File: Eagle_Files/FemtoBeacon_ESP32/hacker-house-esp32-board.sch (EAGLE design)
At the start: 56 parts, among them IC1 FT232RQ

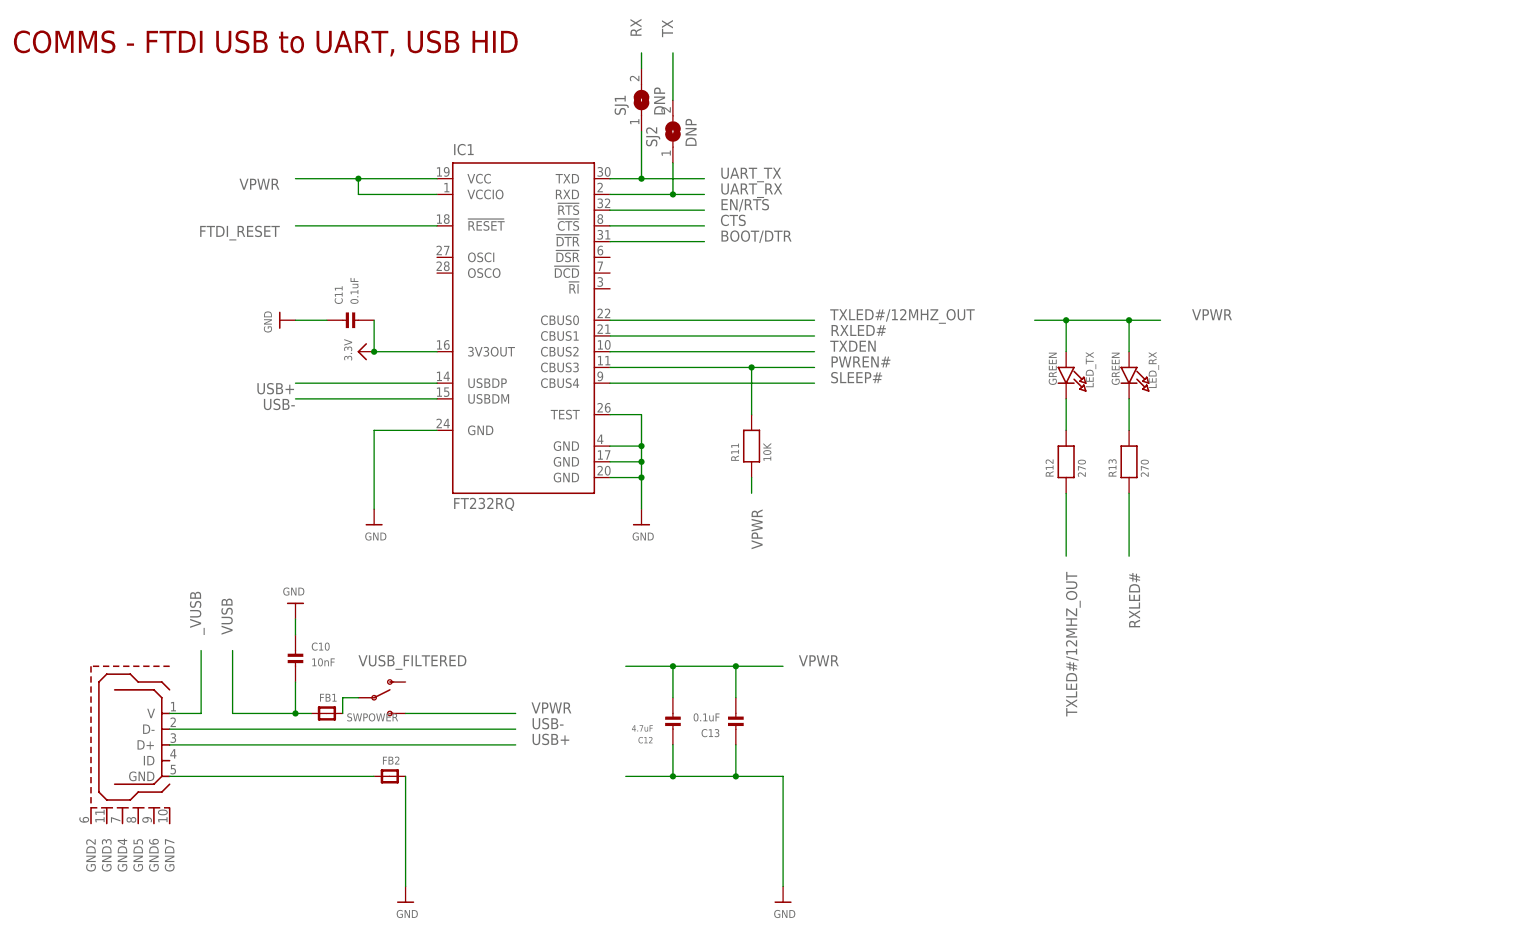
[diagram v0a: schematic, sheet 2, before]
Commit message: Revised BoM for the Hacker.House board, fixed missing 3V3 trace with 2.0.1 design of Hacker.House board (version bump to 2.0.2)
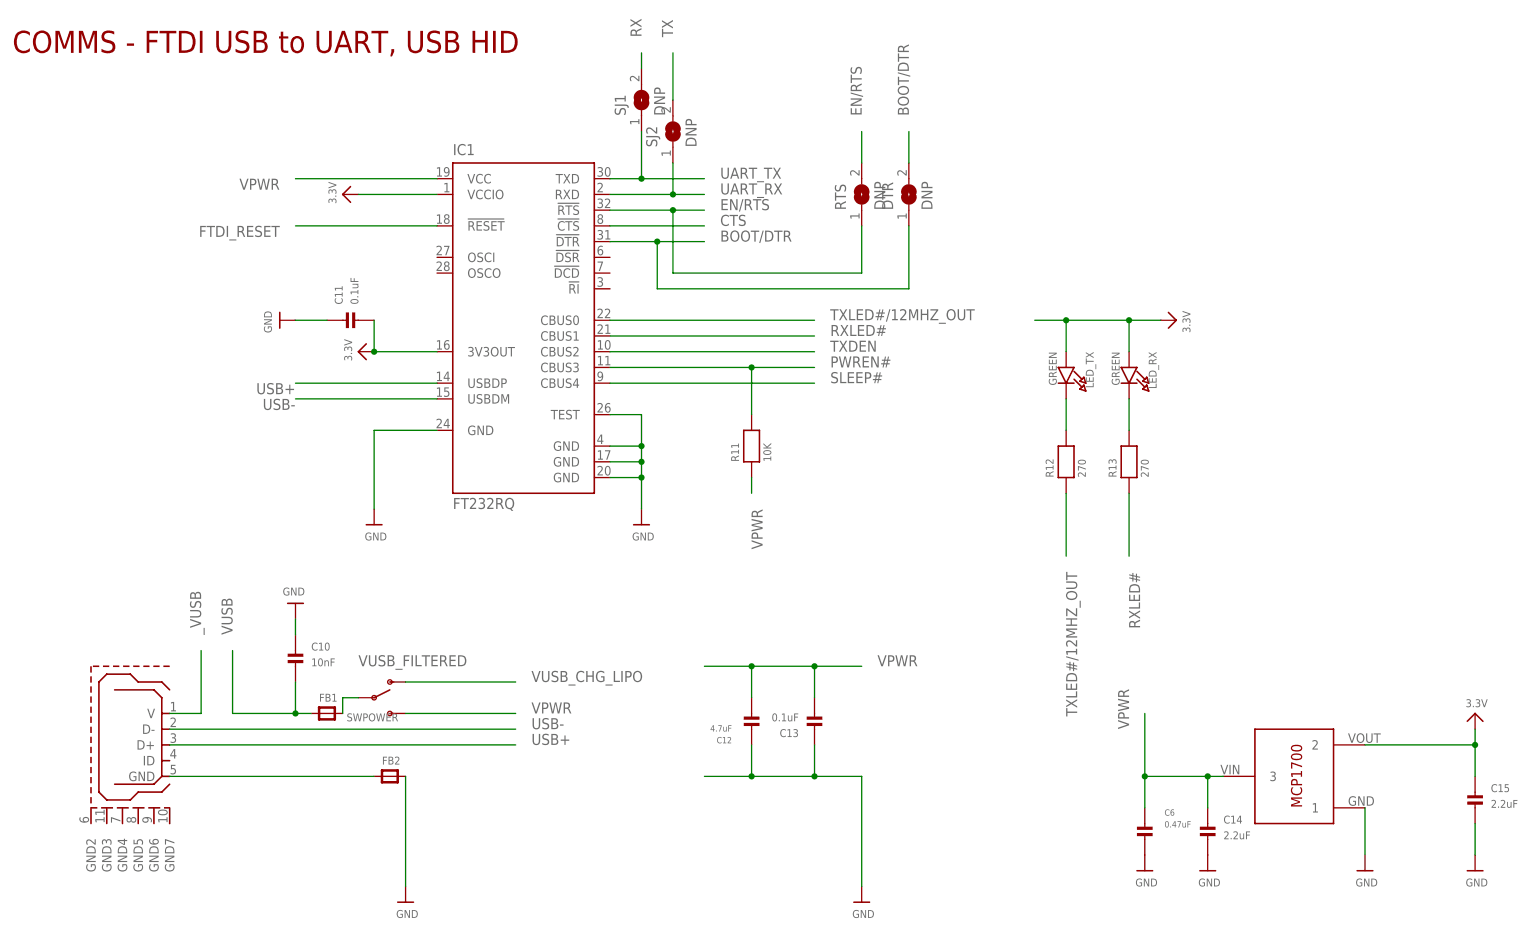
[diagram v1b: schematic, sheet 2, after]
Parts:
- added C14, C15: 2.2uF, microbuilder:CAP_CERAMIC_0402MP
- added C6: 0.47uF, microbuilder:CAP_CERAMIC_0402MP
- added DTR, RTS: DNP, microbuilder:SOLDERJUMPERCLOSED
- added LDO2: 3.3V, MCP1700T-3302E_TT:MCP1700T-3302E/TT
- MOD1: device esp32-wroom-32:ESP32-WROOM-32 -> esp32-wroom-32-managed:ESP32-WROOM-32; MPN (none) -> ESP32-WROOM-32D
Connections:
- removed net GND: BOOT.2, C1.P$2, C10.P$1, C11.P$1, C12.P$1, C13.P$1, C2.P$2, C3.P$2, C4.P$2, C5.P$2, C7.P$1, C8.P$1, C9.P$1, CN_LIPO.1, FB2.P$2, IC1.GND, IC1.GND@1, IC1.GND@2, IC1.GND@A, IC1.TEST, JTAG/HSPI.1, LDO1.1, LED_OK.C, LIPO1.VSS@1, LIPO1.VSS@2, MOD1.GND@1, MOD1.GND@2, MOD1.GND@3, MOD1.GND@4, PCHAN1.G1, PCHAN1.G2, PCHAN2.G1, PCHAN2.G2, POWER.1, POWER.7, POWER.8, R4.2, UART.1
- removed net VCC: C7.P$2, C8.P$2, MOD1.3V3
- new net GND_UNMASKED: BOOT.2, C1.P$2, C10.P$1, C11.P$1, C12.P$1, C13.P$1, C14.P$2, C15.P$2, C2.P$2, C3.P$2, C4.P$2, C5.P$2, C6.P$2, C7.P$1, C8.P$1, C9.P$1, CN_LIPO.1, FB2.P$2, IC1.GND, IC1.GND@1, IC1.GND@2, IC1.GND@A, IC1.TEST, JTAG/HSPI.1, LDO1.1, LDO2.1, LED_OK.C, LIPO1.VSS@1, LIPO1.VSS@2, MOD1.GND@1, MOD1.GND@2, MOD1.GND@3, MOD1.GND@4, PCHAN1.G1, PCHAN1.G2, PCHAN2.G1, PCHAN2.G2, POWER.1, POWER.7, POWER.8, R4.2, UART.1
- new net VUSB_CHG_LIPO: C4.P$1, LED_CHG.A, LIPO1.VDD@1, LIPO1.VDD@2, SWPOWER.O
- net 3.3V: now also C15.P$1, C7.P$2, C8.P$2, IC1.VCCIO, LDO2.2, LED_RX.A, LED_TX.A, MOD1.3V3
- net BOOT/DTR: now also DTR.1, DTR.2
- net EN/RTS: now also RTS.1, RTS.2
- net VPWR: now also C14.P$1, C6.P$1, LDO2.3; no longer IC1.VCCIO, LED_RX.A, LED_TX.A
- net VUSB: no longer C4.P$1, LED_CHG.A, LIPO1.VDD@1, LIPO1.VDD@2
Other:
- moved on the sheet: C1, C12, C13

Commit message: Updating BoM for Hacker.House board. Using ESP32-WROOM-32D (16MB) variant
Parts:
- MOD1: MPN ESP32-WROOM-32D -> ESP32-WROOM-32D (16MB)
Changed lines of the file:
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@@
 <part name="FRAME1" library="frames" library_urn="urn:adsk.eagle:library:229" deviceset="LETTER_L" device=""/>
 <part name="MOD1" library="esp32-wroom-32-managed" library_urn="urn:adsk.eagle:library:11837532" deviceset="ESP32-WROOM-32" device="" package3d_urn="urn:adsk.eagle:package:11837542/1">
-<attribute name="MPN" value="ESP32-WROOM-32D"/>
+<attribute name="MPN" value="ESP32-WROOM-32D (16MB)"/>
 </part>
 <part name="LDO1" library="MCP1700T-3302E_TT" deviceset="MCP1700T-3302E/TT" device="" value="3.3V"/>
